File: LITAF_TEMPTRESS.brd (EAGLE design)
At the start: 5.8 x 25.4 mm, 10 parts, among them T1 TMP117, T2 TMP117, U1 NTAG5_LINK_NTP53X2

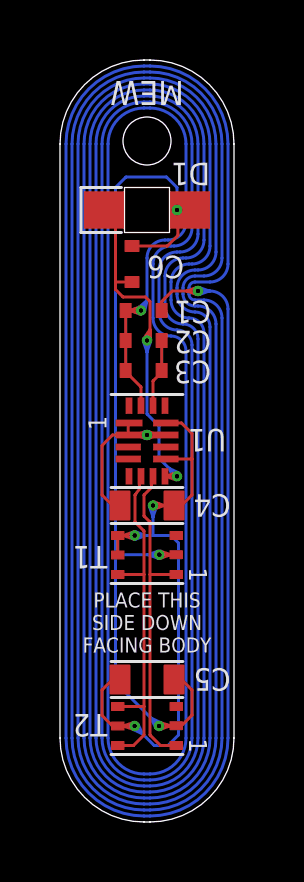
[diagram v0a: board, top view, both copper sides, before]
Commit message: Added current limiting resistor for LED
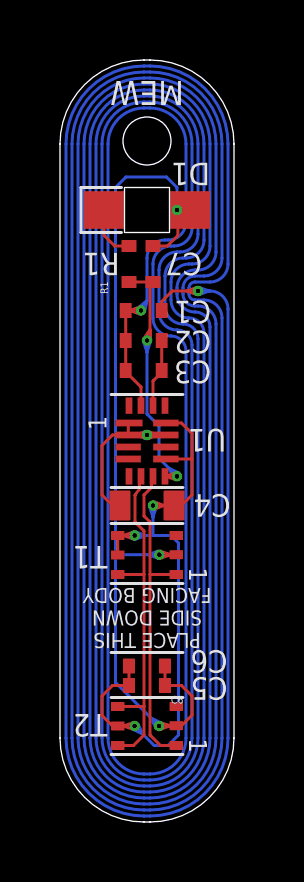
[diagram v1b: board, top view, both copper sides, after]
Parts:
- added C7, R1: (no value), LITAF_TEMPTRESS:0402-SMT
- C5: device LITAF_TEMPTRESS:0603-SMT[WIDE] -> LITAF_TEMPTRESS:0402-SMT
- moved C6 13.4 mm to (2.90, 5.20), turned to 180 degrees
- moved C5 6.00 mm to (2.90, 4.55), turned to 180 degrees
- moved C4 5.80 mm to (2.90, 10.6), turned to 0 degrees
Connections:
- new net N$1: D1.P$1, R1.P$2
- net GND: now also C6.P$1, C7.P$2; no longer C6.P$2
- net LED: now also C7.P$1, R1.P$1; no longer C6.P$1, D1.P$1
- net VOUT: now also C6.P$2
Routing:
- net LED: track 15.2 -> 12.0 mm
- net N$1: track 0.00 -> 1.85 mm
- net VOUT: track 26.0 -> 26.8 mm
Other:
- board text added: "C7"
- board text added: "R1"
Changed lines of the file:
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@@
 <setting verticaltext="up"/>
 </settings>
-<grid distance="0.001" unitdist="mm" unit="mm" style="dots" multiple="1" display="yes" altdistance="0.05" altunitdist="mm" altunit="mm"/>
+<grid distance="0.1" unitdist="mm" unit="mm" style="dots" multiple="1" display="yes" altdistance="0.05" altunitdist="mm" altunit="mm"/>
 <layers>
 <layer number="1" name="Top" color="4" fill="1" visible="yes" active="yes"/>
@@
 .... --- - | .. -. | .... . .-. .</text>
 <text x="2.9" y="24.7" size="0.8" layer="21" ratio="15" rot="SR180" align="bottom-center">MEW</text>
-<text x="2.9" y="5.65" size="0.5" layer="21" ratio="15" align="bottom-center">PLACE THIS
+<text x="2.9" y="7.8" size="0.5" layer="21" ratio="15" rot="SR180" align="bottom-center">PLACE THIS
 SIDE DOWN
 FACING BODY</text>
 <text x="1.6" y="20.38" size="1" layer="26" ratio="15" rot="SMR270" align="bottom-center">LITAF</text>
 <wire x1="1.7" y1="9.95" x2="4.1" y2="9.95" width="0.1" layer="21"/>
-<wire x1="1.7" y1="5.35" x2="4.1" y2="5.35" width="0.1" layer="21"/>
+<wire x1="1.7" y1="5.65" x2="4.1" y2="5.65" width="0.1" layer="21"/>
 <text x="4.45" y="10.55" size="0.75" layer="21" ratio="10" rot="SR180" align="center-right">C4</text>
-<text x="4.45" y="4.75" size="0.75" layer="21" ratio="10" rot="SR180" align="center-right">C5</text>
-<text x="2.9" y="18.5" size="0.75" layer="21" ratio="10" rot="SR180" align="center-right">C6</text>
+<text x="4.35" y="4.45" size="0.75" layer="21" ratio="10" rot="SR180" align="center-right">C5</text>
+<text x="3.5" y="18.6" size="0.75" layer="21" ratio="10" rot="SR180" align="center-right">C7</text>
 <text x="3.7" y="21.6" size="0.75" layer="21" ratio="10" rot="SR180" align="center-right">D1</text>
 <text x="1" y="3.6" size="0.75" layer="21" ratio="10" rot="SR180" align="bottom-center">T2</text>
+<text x="4.35" y="5.35" size="0.75" layer="21" ratio="10" rot="SR180" align="center-right">C6</text>
+<text x="0.75" y="18.6" size="0.75" layer="21" ratio="10" rot="SR180" align="center-right">R1</text>
 </plain>
 <attributes>
@@
 <element name="T2" library="LITAF_TEMPTRESS" package="DRV0006B" value="TMP117" x="2.9" y="3.2" smashed="yes" rot="R180"/>
 <element name="D1" library="LITAF_TEMPTRESS" package="IN-S124AR" value="IN-S124AR" x="2.9" y="20.4" smashed="yes"/>
-<element name="C4" library="LITAF_TEMPTRESS" package="0603-SMT[WIDE]" value="" x="2.9" y="4.75" smashed="yes" rot="R180">
-<attribute name="VALUE" x="3.9" y="4.25" size="0.15" layer="27" rot="R180"/>
+<element name="C5" library="LITAF_TEMPTRESS" package="0402-SMT" value="" x="2.9" y="4.55" smashed="yes" rot="R180">
+<attribute name="VALUE" x="3.9" y="4.05" size="0.15" layer="27" rot="R180"/>
 </element>
-<element name="C5" library="LITAF_TEMPTRESS" package="0603-SMT[WIDE]" value="" x="2.9" y="10.55" smashed="yes">
+<element name="C4" library="LITAF_TEMPTRESS" package="0603-SMT[WIDE]" value="" x="2.9" y="10.55" smashed="yes">
 <attribute name="VALUE" x="1.9" y="11.05" size="0.15" layer="27"/>
 </element>
-<element name="C6" library="LITAF_TEMPTRESS" package="0402-SMT" value="" x="2.4" y="18.6" smashed="yes" rot="R90">
-<attribute name="VALUE" x="1.9" y="17.6" size="0.15" layer="27" rot="R90"/>
+<element name="C7" library="LITAF_TEMPTRESS" package="0402-SMT" value="" x="3.1" y="18.6" smashed="yes" rot="R90">
+<attribute name="VALUE" x="2.6" y="17.6" size="0.15" layer="27" rot="R90"/>
+</element>
+<element name="R1" library="LITAF_TEMPTRESS" package="0402-SMT" value="" x="2.3" y="18.6" smashed="yes" rot="R90">
+<attribute name="NAME" x="1.6" y="17.6" size="0.254" layer="25" rot="R90"/>
+<attribute name="NAME" x="1.6" y="17.6" size="0.254" layer="25" rot="R90"/>
+<attribute name="VALUE" x="1.8" y="17.6" size="0.15" layer="27" rot="R90"/>
+<attribute name="VALUE" x="1.8" y="17.6" size="0.15" layer="27" rot="R90"/>
+</element>
+<element name="C6" library="LITAF_TEMPTRESS" package="0402-SMT" value="" x="2.9" y="5.2" smashed="yes" rot="R180">
+<attribute name="NAME" x="4.114" y="4.202" size="0.254" layer="25" rot="R180"/>
+<attribute name="VALUE" x="4.1" y="4.4" size="0.15" layer="27" rot="R180"/>
 </element>
 </elements>
@@
 <contactref element="U1" pad="P$12"/>
 <contactref element="U1" pad="P$9"/>
+<contactref element="C5" pad="P$2"/>
 <contactref element="C4" pad="P$2"/>
-<contactref element="C5" pad="P$2"/>
 <contactref element="T1" pad="P4"/>
 <wire x1="1.925" y1="9.55" x2="1.925" y2="8.9" width="0.1" layer="1"/>
@@
 <wire x1="1.925" y1="3.2" x2="1.75" y2="3.2" width="0.1" layer="1"/>
 <wire x1="1.75" y1="3.2" x2="1.4" y2="3.55" width="0.1" layer="1"/>
-<wire x1="1.4" y1="3.55" x2="1.4" y2="4.4" width="0.1" layer="1"/>
-<wire x1="1.4" y1="4.4" x2="1.75" y2="4.75" width="0.1" layer="1"/>
-<wire x1="1.75" y1="4.75" x2="2" y2="4.75" width="0.1" layer="1"/>
 <wire x1="2.49" y1="3.2" x2="2.755165625" y2="2.934834375" width="0.1" layer="16"/>
 <wire x1="2.755165625" y1="2.934834375" x2="3.14" y2="2.55" width="0.1" layer="16"/>
@@
 <wire x1="3.1" y1="10.174996875" x2="2.982146875" y2="10.508328125" width="0.1" layer="16"/>
 <wire x1="3.1" y1="10.55" x2="2.982146875" y2="10.508328125" width="0.1" layer="16"/>
+<contactref element="C6" pad="P$2"/>
+<wire x1="1.4" y1="3.55" x2="1.4" y2="4.2" width="0.1" layer="1"/>
+<wire x1="1.4" y1="4.2" x2="1.75" y2="4.55" width="0.1" layer="1"/>
+<wire x1="1.75" y1="4.55" x2="2.3" y2="4.55" width="0.1" layer="1"/>
+<wire x1="2.3" y1="4.55" x2="2.3" y2="5.2" width="0.1" layer="1"/>
 </signal>
 <signal name="GND">
@@
 <contactref element="U1" pad="P$2"/>
 <contactref element="U1" pad="P$1"/>
+<contactref element="C5" pad="P$1"/>
 <contactref element="C4" pad="P$1"/>
-<contactref element="C5" pad="P$1"/>
 <wire x1="3.525" y1="12.9" x2="3.275003125" y2="12.9" width="0.1" layer="1"/>
 <wire x1="3.275003125" y1="12.9" x2="2.9" y2="12.9" width="0.1" layer="1"/>
@@
 <wire x1="1.75" y1="12.9" x2="1.4" y2="12.55" width="0.1" layer="1"/>
 <wire x1="3.875" y1="3.21" x2="4.05" y2="3.21" width="0.1" layer="1"/>
-<wire x1="4.05" y1="3.21" x2="4.4" y2="3.56" width="0.1" layer="1"/>
-<wire x1="4.4" y1="3.56" x2="4.4" y2="4.4" width="0.1" layer="1"/>
-<wire x1="4.4" y1="4.4" x2="4.05" y2="4.75" width="0.1" layer="1"/>
-<wire x1="4.05" y1="4.75" x2="3.8" y2="4.75" width="0.1" layer="1"/>
+<wire x1="4.4" y1="3.56" x2="4.05" y2="3.21" width="0.1" layer="1"/>
 <wire x1="1.85" y1="8.91" x2="1.85" y2="4.65" width="0.1" layer="16"/>
 <wire x1="1.85" y1="4.65" x2="3.034834375" y2="3.465165625" width="0.1" layer="16"/>
@@
 <wire x1="4.275003125" y1="20.4" x2="3.9" y2="20.4" width="0.1" layer="1"/>
 <wire x1="2.9" y1="12.9" x2="2.524996875" y2="12.9" width="0.1" layer="1"/>
-<contactref element="C6" pad="P$2"/>
+<contactref element="C7" pad="P$2"/>
 <wire x1="2.524996875" y1="12.9" x2="2.275" y2="12.9" width="0.1" layer="1"/>
 <wire x1="3.93" y1="20" x2="3.93" y2="19.55" width="0.1" layer="1"/>
 <wire x1="3.93" y1="19.55" x2="3.58" y2="19.2" width="0.1" layer="1"/>
-<wire x1="3.58" y1="19.2" x2="2.4" y2="19.2" width="0.1" layer="1"/>
 <wire x1="3.93" y1="20" x2="4.33" y2="20.4" width="0.1" layer="1"/>
 <wire x1="3.275003125" y1="12.9" x2="2.94166875" y2="13.01785" width="0.1" layer="1"/>
@@
 <wire x1="3.034834375" y1="3.465165625" x2="3.35386875" y2="3.31279375" width="0.1" layer="16"/>
 <wire x1="3.3" y1="3.2" x2="3.35386875" y2="3.31279375" width="0.1" layer="16"/>
+<wire x1="3.58" y1="19.2" x2="3.1" y2="19.2" width="0.1" layer="1"/>
+<contactref element="C6" pad="P$1"/>
+<wire x1="3.5" y1="4.55" x2="4.05" y2="4.55" width="0.1" layer="1"/>
+<wire x1="4.05" y1="4.55" x2="4.4" y2="4.2" width="0.1" layer="1"/>
+<wire x1="4.4" y1="4.2" x2="4.4" y2="3.56" width="0.1" layer="1"/>
+<wire x1="3.5" y1="4.55" x2="3.5" y2="5.2" width="0.1" layer="1"/>
 </signal>
 <signal name="SCL">
@@
 <signal name="LED">
 <contactref element="U1" pad="P$8"/>
-<wire x1="2.1" y1="17.5" x2="1.85" y2="17.75" width="0.1" layer="1"/>
-<wire x1="2.1" y1="17.5" x2="2.85" y2="17.5" width="0.1" layer="1"/>
-<wire x1="2.85" y1="17.5" x2="3" y2="17.35" width="0.1" layer="1"/>
-<wire x1="3" y1="17.35" x2="3" y2="16.411421875" width="0.1" layer="1"/>
 <via x="2.9" y="16.05" extent="1-16" drill="0.15"/>
 <wire x1="3" y1="16.3" x2="3" y2="16.411421875" width="0.1" layer="1"/>
 <via x="3.9" y="11.525" extent="1-16" drill="0.15"/>
-<contactref element="D1" pad="P$1"/>
-<wire x1="1.85" y1="17.75" x2="1.85" y2="18" width="0.1" layer="1"/>
-<wire x1="1.85" y1="18" x2="1.85" y2="19.95" width="0.1" layer="1"/>
-<wire x1="1.85" y1="19.95" x2="1.9" y2="20" width="0.1" layer="1"/>
-<wire x1="1.9" y1="20" x2="1.5" y2="20.4" width="0.1" layer="1"/>
-<wire x1="1.5" y1="20.4" x2="1.47" y2="20.4" width="0.1" layer="1"/>
 <wire x1="3.5" y1="11.525" x2="3.524996875" y2="11.525" width="0.1" layer="1"/>
-<contactref element="C6" pad="P$1"/>
+<contactref element="C7" pad="P$1"/>
 <wire x1="3.524996875" y1="11.525" x2="3.9" y2="11.525" width="0.1" layer="1"/>
-<wire x1="2.4" y1="18" x2="1.85" y2="18" width="0.1" layer="1"/>
 <wire x1="2.9" y1="16.05" x2="2.9" y2="15.674996875" width="0.1" layer="16"/>
 <wire x1="2.9" y1="15.674996875" x2="2.9" y2="13.6" width="0.1" layer="16"/>
@@
 <wire x1="3.9" y1="11.525" x2="3.95386875" y2="11.63779375" width="0.1" layer="16"/>
 <wire x1="2.9" y1="16.05" x2="3" y2="16.3" width="0.1" layer="1"/>
+<contactref element="R1" pad="P$1"/>
+<wire x1="3" y1="18" x2="3.1" y2="18" width="0.1" layer="1"/>
+<wire x1="3" y1="16.411421875" x2="3" y2="18" width="0.1" layer="1"/>
+<wire x1="3.1" y1="18" x2="2.3" y2="18" width="0.1" layer="1"/>
+</signal>
+<signal name="N$1">
+<contactref element="D1" pad="P$1"/>
+<contactref element="R1" pad="P$2"/>
+<wire x1="1.5" y1="20.4" x2="1.47" y2="20.4" width="0.1" layer="1"/>
+<wire x1="1.47" y1="20.4" x2="1.47" y2="19.55" width="0.1" layer="1"/>
+<wire x1="1.47" y1="19.55" x2="1.82" y2="19.2" width="0.1" layer="1"/>
+<wire x1="1.82" y1="19.2" x2="2.3" y2="19.2" width="0.1" layer="1"/>
 </signal>
 </signals>
